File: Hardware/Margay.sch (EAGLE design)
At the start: 70 parts, among them IC1 ATMEGA644M, J1 CONN_42.54_SCREW, J2 CONN_6SCREW_2.54, Q1 FDN360P, Q2 DMG3404, Q3 2N7002, Q4 FDN360P, Q6 FDN360P, U2 FT231X-Q

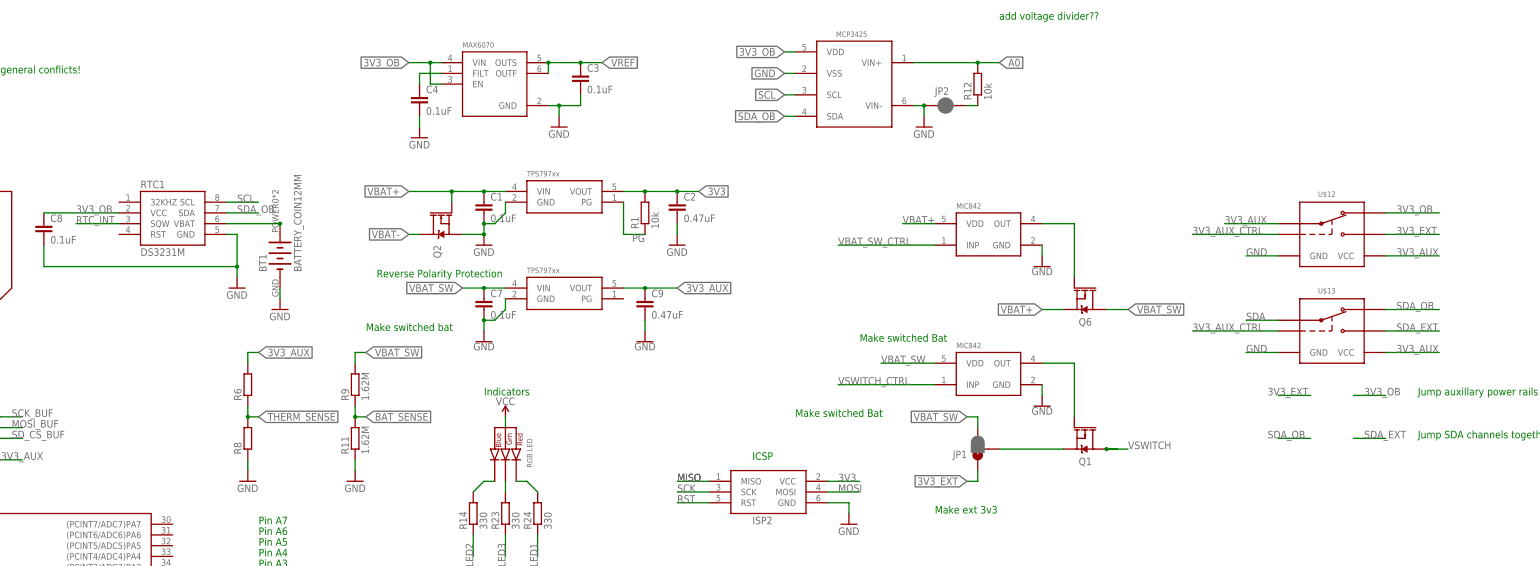
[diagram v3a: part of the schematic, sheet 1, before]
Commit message: Cleaned up board, removed power switch
Cleaned up the routing, removed the switched power
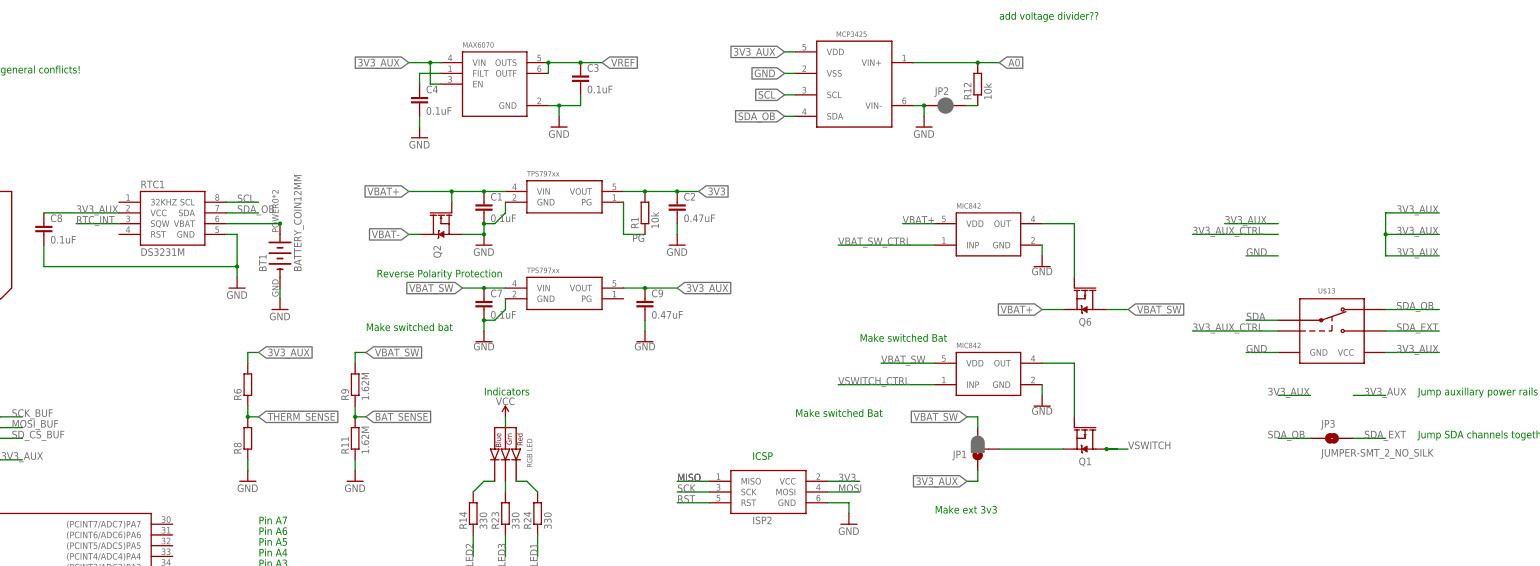
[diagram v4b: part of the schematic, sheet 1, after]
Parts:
- removed U$12: SN74LVC1G3157DRL, bschulz:SN74LVC1G3157DRL
- added JP3: JUMPER-SMT_2_NO_SILK, SparkFun-Jumpers:JUMPER-SMT_2_NO_SILK
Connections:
- removed net 3V3_EXT: J1.3, J2.2, JP1.1, U$12.B2
- removed net 3V3_OB: C8.1, RTC1.VCC, U$12.B1, U$7.EN, U$7.VIN, U$8.VDD
- net 3V3_AUX: now also C8.1, J1.3, J2.2, JP1.1, RTC1.VCC, U$7.EN, U$7.VIN, U$8.VDD; no longer U$12.A, U$12.VCC
- net 3V3_AUX_CTRL: no longer U$12.S
- net GND: no longer U$12.GND
- net SDA_EXT: now also JP3.2
- net SDA_OB: now also JP3.1
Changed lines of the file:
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@@
 <part name="U$11" library="bschulz" deviceset="MIC842" device="" technology="H" value="MIC842H"/>
 <part name="GND15" library="SparkFun-PowerSymbols" library_urn="urn:adsk.eagle:library:530" deviceset="GND" device=""/>
-<part name="U$12" library="bschulz" deviceset="SN74LVC1G3157" device="DRL"/>
 <part name="U$13" library="bschulz" deviceset="SN74LVC1G3157" device="DRL"/>
 <part name="U$17" library="bschulz" deviceset="SN74AUP3G34" device="DCU"/>
+<part name="JP3" library="SparkFun-Jumpers" library_urn="urn:adsk.eagle:library:528" deviceset="JUMPER-SMT_2_NO" device="_SILK" package3d_urn="urn:adsk.eagle:package:39279/1"/>
 </parts>
 <sheets>
@@
 <instance part="U$11" gate="G$1" x="322.58" y="180.34"/>
 <instance part="GND15" gate="1" x="337.82" y="172.72"/>
-<instance part="U$12" gate="G$1" x="406.4" y="182.88"/>
 <instance part="U$13" gate="G$1" x="406.4" y="160.02"/>
 <instance part="U$17" gate="G$1" x="78.74" y="132.08"/>
+<instance part="JP3" gate="G$1" x="406.4" y="132.08"/>
 </instances>
 <busses>
@@
 </segment>
 <segment>
-<pinref part="U$12" gate="G$1" pin="GND"/>
 <wire x1="393.7" y1="175.26" x2="386.08" y2="175.26" width="0.1524" layer="91"/>
 <label x="386.08" y="175.26" size="1.778" layer="95"/>
@@
 </segment>
 <segment>
-<pinref part="U$12" gate="G$1" pin="VCC"/>
 <wire x1="419.1" y1="175.26" x2="431.8" y2="175.26" width="0.1524" layer="91"/>
 <label x="421.64" y="175.26" size="1.778" layer="95"/>
+<wire x1="419.1" y1="185.42" x2="431.8" y2="185.42" width="0.1524" layer="91"/>
+<label x="421.64" y="185.42" size="1.778" layer="95"/>
+<wire x1="419.1" y1="180.34" x2="431.8" y2="180.34" width="0.1524" layer="91"/>
+<label x="421.64" y="180.34" size="1.778" layer="95"/>
+<wire x1="419.1" y1="185.42" x2="419.1" y2="180.34" width="0.1524" layer="91"/>
+<wire x1="419.1" y1="175.26" x2="419.1" y2="180.34" width="0.1524" layer="91"/>
+<junction x="419.1" y="180.34"/>
 </segment>
 <segment>
@@
 </segment>
 <segment>
-<pinref part="U$12" gate="G$1" pin="A"/>
 <wire x1="393.7" y1="182.88" x2="381" y2="182.88" width="0.1524" layer="91"/>
 <label x="381" y="182.88" size="1.778" layer="95"/>
@@
 <label x="40.64" y="172.72" size="1.778" layer="95" rot="R180" xref="yes"/>
 </segment>
-</net>
-<net name="N$4" class="0">
-<segment>
-<pinref part="U$11" gate="G$1" pin="OUT"/>
-<pinref part="Q6" gate="G$1" pin="G"/>
-<wire x1="337.82" y1="182.88" x2="345.44" y2="182.88" width="0.1524" layer="91"/>
-<wire x1="345.44" y1="182.88" x2="345.44" y2="170.18" width="0.1524" layer="91"/>
-</segment>
-</net>
-<net name="VBAT_SW_CTRL" class="0">
-<segment>
-<pinref part="U$11" gate="G$1" pin="INP"/>
-<wire x1="312.42" y1="177.8" x2="289.56" y2="177.8" width="0.1524" layer="91"/>
-<label x="289.56" y="177.8" size="1.778" layer="95"/>
-</segment>
-<segment>
-<pinref part="IC1" gate="G$1" pin="(PCINT19/TMS)PC3"/>
-<wire x1="132.08" y1="55.88" x2="142.24" y2="55.88" width="0.1524" layer="91"/>
-<label x="137.16" y="55.88" size="1.778" layer="95"/>
-</segment>
-</net>
-<net name="3V3_OB" class="0">
 <segment>
 <pinref part="RTC1" gate="G$1" pin="VCC"/>
@@
 </segment>
 <segment>
-<pinref part="U$12" gate="G$1" pin="B1"/>
-<wire x1="419.1" y1="185.42" x2="431.8" y2="185.42" width="0.1524" layer="91"/>
-<label x="421.64" y="185.42" size="1.778" layer="95"/>
-</segment>
-<segment>
 <wire x1="411.48" y1="142.24" x2="419.1" y2="142.24" width="0.1524" layer="91"/>
 <label x="414.02" y="142.24" size="1.778" layer="95"/>
-</segment>
-</net>
-<net name="3V3_AUX_CTRL" class="0">
-<segment>
-<pinref part="U$12" gate="G$1" pin="S"/>
-<wire x1="393.7" y1="180.34" x2="373.38" y2="180.34" width="0.1524" layer="91"/>
-<label x="373.38" y="180.34" size="1.778" layer="95"/>
-</segment>
-<segment>
-<pinref part="U$13" gate="G$1" pin="S"/>
-<wire x1="393.7" y1="157.48" x2="373.38" y2="157.48" width="0.1524" layer="91"/>
-<label x="373.38" y="157.48" size="1.778" layer="95"/>
-</segment>
-<segment>
-<pinref part="IC1" gate="G$1" pin="(PCINT28/OC1B)PD4"/>
-<wire x1="132.08" y1="35.56" x2="142.24" y2="35.56" width="0.1524" layer="91"/>
-<label x="137.16" y="35.56" size="1.778" layer="95"/>
-</segment>
-</net>
-<net name="SDA_EXT" class="0">
-<segment>
-<pinref part="U$13" gate="G$1" pin="B2"/>
-<wire x1="419.1" y1="157.48" x2="431.8" y2="157.48" width="0.1524" layer="91"/>
-<label x="421.64" y="157.48" size="1.778" layer="95"/>
-</segment>
-<segment>
-<wire x1="411.48" y1="132.08" x2="419.1" y2="132.08" width="0.1524" layer="91"/>
-<label x="414.02" y="132.08" size="1.778" layer="95"/>
-</segment>
-</net>
-<net name="SDA_OB" class="0">
-<segment>
-<pinref part="U$13" gate="G$1" pin="B1"/>
-<wire x1="419.1" y1="162.56" x2="431.8" y2="162.56" width="0.1524" layer="91"/>
-<label x="421.64" y="162.56" size="1.778" layer="95"/>
-</segment>
-<segment>
-<pinref part="RTC1" gate="G$1" pin="SDA"/>
-<wire x1="144.78" y1="185.42" x2="152.4" y2="185.42" width="0.1524" layer="91"/>
-<label x="147.32" y="185.42" size="1.778" layer="95"/>
-</segment>
-<segment>
-<pinref part="U$8" gate="G$1" pin="SDA"/>
-<wire x1="279.4" y1="208.28" x2="276.86" y2="208.28" width="0.1524" layer="91"/>
-<label x="276.86" y="208.28" size="1.778" layer="95" rot="R180" xref="yes"/>
-</segment>
-<segment>
-<wire x1="401.32" y1="132.08" x2="393.7" y2="132.08" width="0.1524" layer="91"/>
-<label x="391.16" y="132.08" size="1.778" layer="95"/>
-</segment>
-</net>
-<net name="3V3_EXT" class="0">
-<segment>
-<pinref part="U$12" gate="G$1" pin="B2"/>
-<wire x1="419.1" y1="180.34" x2="431.8" y2="180.34" width="0.1524" layer="91"/>
-<label x="421.64" y="180.34" size="1.778" layer="95"/>
 </segment>
 <segment>
@@
 <wire x1="322.58" y1="121.92" x2="320.04" y2="121.92" width="0.1524" layer="91"/>
 <label x="320.04" y="121.92" size="1.778" layer="95" rot="R180" xref="yes"/>
+</segment>
+</net>
+<net name="N$4" class="0">
+<segment>
+<pinref part="U$11" gate="G$1" pin="OUT"/>
+<pinref part="Q6" gate="G$1" pin="G"/>
+<wire x1="337.82" y1="182.88" x2="345.44" y2="182.88" width="0.1524" layer="91"/>
+<wire x1="345.44" y1="182.88" x2="345.44" y2="170.18" width="0.1524" layer="91"/>
+</segment>
+</net>
+<net name="VBAT_SW_CTRL" class="0">
+<segment>
+<pinref part="U$11" gate="G$1" pin="INP"/>
+<wire x1="312.42" y1="177.8" x2="289.56" y2="177.8" width="0.1524" layer="91"/>
+<label x="289.56" y="177.8" size="1.778" layer="95"/>
+</segment>
+<segment>
+<pinref part="IC1" gate="G$1" pin="(PCINT19/TMS)PC3"/>
+<wire x1="132.08" y1="55.88" x2="142.24" y2="55.88" width="0.1524" layer="91"/>
+<label x="137.16" y="55.88" size="1.778" layer="95"/>
+</segment>
+</net>
+<net name="3V3_AUX_CTRL" class="0">
+<segment>
+<wire x1="393.7" y1="180.34" x2="373.38" y2="180.34" width="0.1524" layer="91"/>
+<label x="373.38" y="180.34" size="1.778" layer="95"/>
+</segment>
+<segment>
+<pinref part="U$13" gate="G$1" pin="S"/>
+<wire x1="393.7" y1="157.48" x2="373.38" y2="157.48" width="0.1524" layer="91"/>
+<label x="373.38" y="157.48" size="1.778" layer="95"/>
+</segment>
+<segment>
+<pinref part="IC1" gate="G$1" pin="(PCINT28/OC1B)PD4"/>
+<wire x1="132.08" y1="35.56" x2="142.24" y2="35.56" width="0.1524" layer="91"/>
+<label x="137.16" y="35.56" size="1.778" layer="95"/>
+</segment>
+</net>
+<net name="SDA_EXT" class="0">
+<segment>
+<pinref part="U$13" gate="G$1" pin="B2"/>
+<wire x1="419.1" y1="157.48" x2="431.8" y2="157.48" width="0.1524" layer="91"/>
+<label x="421.64" y="157.48" size="1.778" layer="95"/>
+</segment>
+<segment>
+<wire x1="411.48" y1="132.08" x2="419.1" y2="132.08" width="0.1524" layer="91"/>
+<label x="414.02" y="132.08" size="1.778" layer="95"/>
+<pinref part="JP3" gate="G$1" pin="2"/>
+</segment>
+</net>
+<net name="SDA_OB" class="0">
+<segment>
+<pinref part="U$13" gate="G$1" pin="B1"/>
+<wire x1="419.1" y1="162.56" x2="431.8" y2="162.56" width="0.1524" layer="91"/>
+<label x="421.64" y="162.56" size="1.778" layer="95"/>
+</segment>
+<segment>
+<pinref part="RTC1" gate="G$1" pin="SDA"/>
+<wire x1="144.78" y1="185.42" x2="152.4" y2="185.42" width="0.1524" layer="91"/>
+<label x="147.32" y="185.42" size="1.778" layer="95"/>
+</segment>
+<segment>
+<pinref part="U$8" gate="G$1" pin="SDA"/>
+<wire x1="279.4" y1="208.28" x2="276.86" y2="208.28" width="0.1524" layer="91"/>
+<label x="276.86" y="208.28" size="1.778" layer="95" rot="R180" xref="yes"/>
+</segment>
+<segment>
+<wire x1="401.32" y1="132.08" x2="393.7" y2="132.08" width="0.1524" layer="91"/>
+<label x="391.16" y="132.08" size="1.778" layer="95"/>
+<pinref part="JP3" gate="G$1" pin="1"/>
 </segment>
 </net>
@@
 </segment>
 </net>
-<net name="3V3_EXT" class="0">
+<net name="3V3_AUX" class="0">
 <segment>
 <pinref part="J2" gate="G$1" pin="2"/>

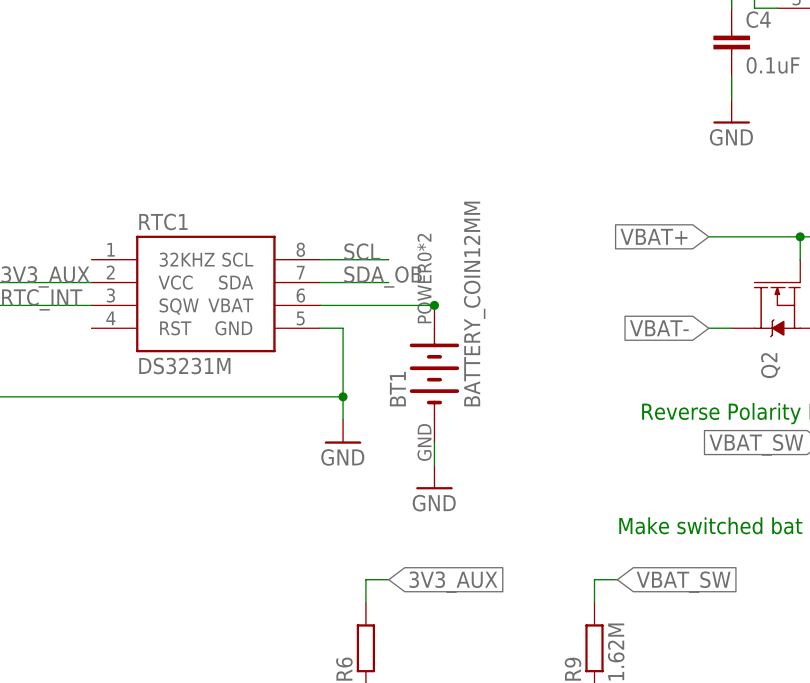
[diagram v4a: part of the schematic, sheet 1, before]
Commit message: Updated board, fixed software logging time
Cleaned up traces on board, changed battery in schematic, updated logging program to have 15 minute interval by default
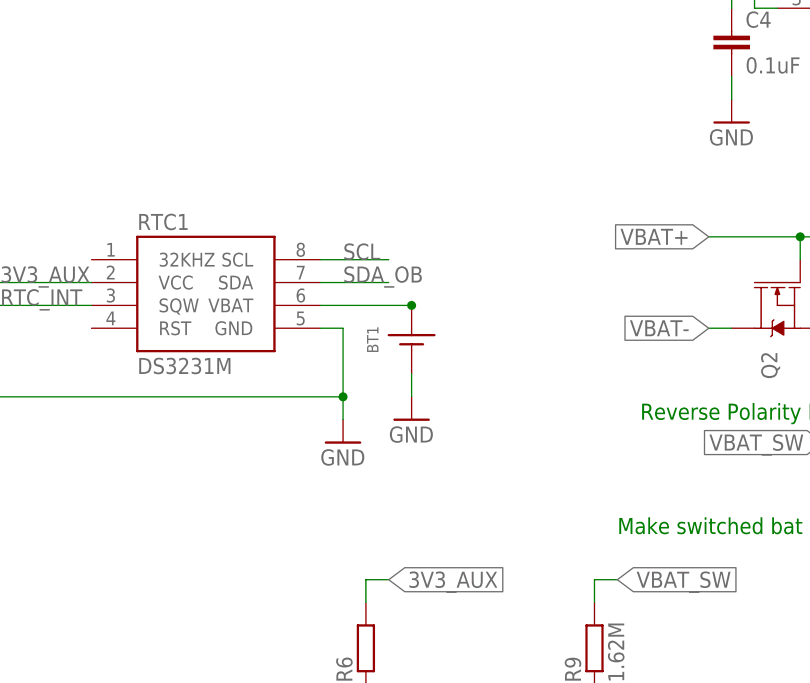
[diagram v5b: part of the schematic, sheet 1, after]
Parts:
- U$1: value CRYSTAL_5X3.2_2LEAD -> CRYSTAL8MHZ5X3.2; device bschulz:CRYSTAL_5X3.2_2LEAD -> bschulz:CRYSTAL8MHZ5X3.2
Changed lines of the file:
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@@
 <part name="SUPPLY47" library="supply2" library_urn="urn:adsk.eagle:library:372" deviceset="GND" device=""/>
 <part name="MICRO_USB" library="bschulz" deviceset="MICRO_USB_LONGPADS" device=""/>
-<part name="U$1" library="bschulz" deviceset="CRYSTAL_5X3.2_2LEAD" device=""/>
+<part name="U$1" library="bschulz" deviceset="CRYSTAL" device="5X3.2" technology="8MHZ" value="CRYSTAL8MHZ5X3.2"/>
 <part name="R4" library="bschulz_passives" deviceset="R-EU_" device="R0603" technology="330" value="330">
 <attribute name="MPN" value="RC0603FR-07330RL"/>
@@
 <instances>
 <instance part="RTC1" gate="G$1" x="132.08" y="182.88"/>
-<instance part="BT1" gate="G$1" x="157.48" y="175.26" rot="R90"/>
-<instance part="GND24" gate="1" x="157.48" y="162.56"/>
+<instance part="BT1" gate="G$1" x="154.94" y="177.8"/>
+<instance part="GND24" gate="1" x="154.94" y="170.18"/>
 <instance part="GND25" gate="1" x="147.32" y="167.64"/>
 <instance part="SUPPLY4" gate="G$1" x="210.82" y="137.16"/>
@@
 <pinref part="GND24" gate="1" pin="GND"/>
 <pinref part="BT1" gate="G$1" pin="-"/>
-<wire x1="157.48" y1="165.1" x2="157.48" y2="167.64" width="0.1524" layer="91"/>
+<wire x1="154.94" y1="172.72" x2="154.94" y2="175.26" width="0.1524" layer="91"/>
 </segment>
 <segment>
@@
 <segment>
 <pinref part="RTC1" gate="G$1" pin="VBAT"/>
-<wire x1="144.78" y1="182.88" x2="157.48" y2="182.88" width="0.1524" layer="91"/>
+<wire x1="144.78" y1="182.88" x2="154.94" y2="182.88" width="0.1524" layer="91"/>
 <pinref part="BT1" gate="G$1" pin="+"/>
-<junction x="157.48" y="182.88"/>
-</segment>
-</net>
+<junction x="154.94" y="182.88"/>
+</segment>
+</net>
